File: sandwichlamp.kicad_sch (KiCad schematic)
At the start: 27 parts, among them J1 Pole1, J2 Pole2, J3 Pole3, J4 12V Enable, J5 HLK-LD2410C, J6 Conn_01x02, J7 Conn_01x03, SW1 Rader Power, SW3 POWER, U1 magnetic-charger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

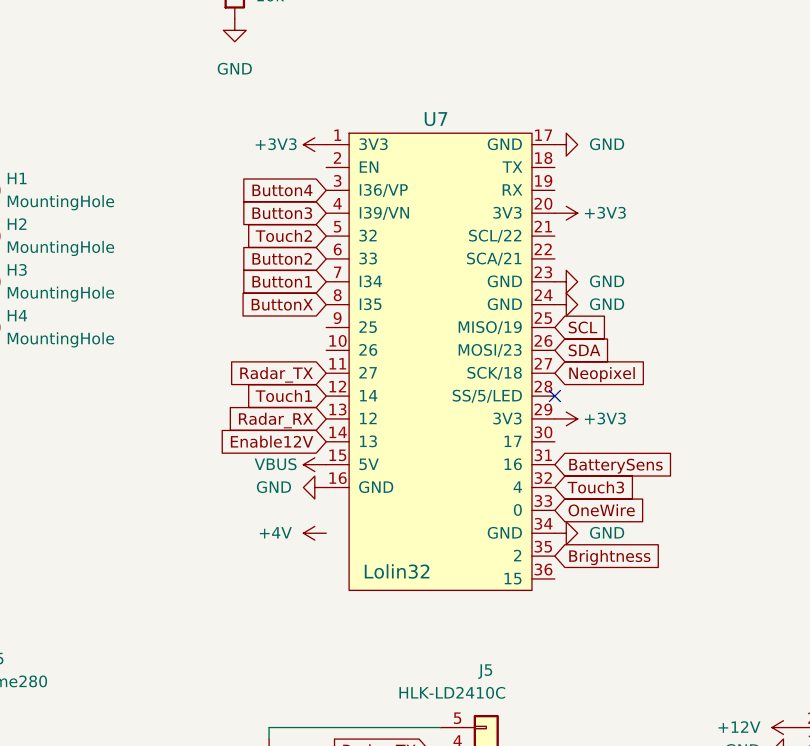
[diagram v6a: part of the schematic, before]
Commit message: Cleanup schematic and pcb
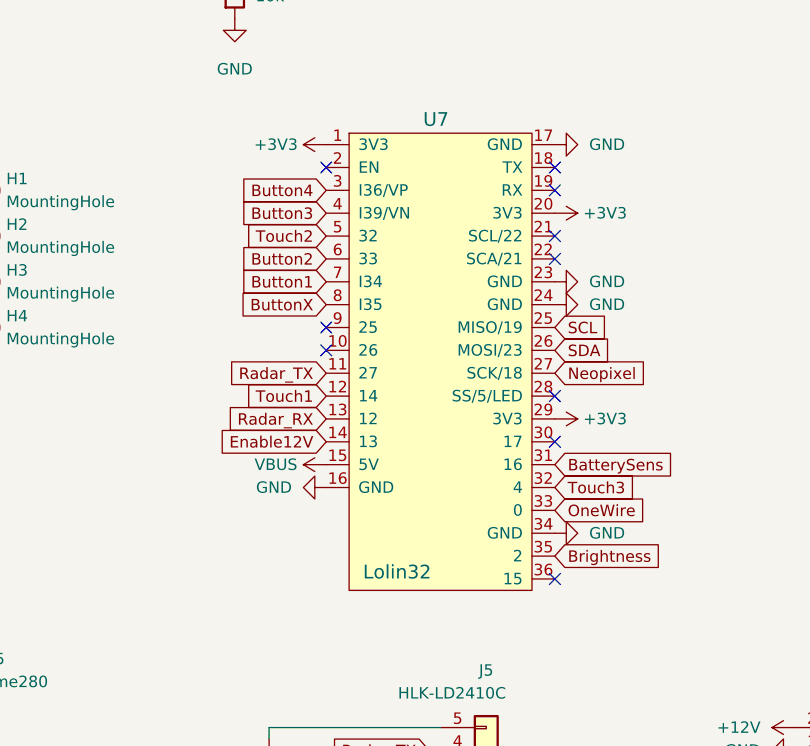
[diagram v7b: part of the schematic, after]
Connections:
- no-connect marks 3 -> 12
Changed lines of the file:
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@@
 	)
 	(no_connect
+		(at 130.81 80.01)
+	)
+	(no_connect
 		(at 31.75 60.96)
 	)
@@
 		(at 156.21 85.09)
 	)
+	(no_connect
+		(at 156.21 105.41)
+	)
+	(no_connect
+		(at 156.21 59.69)
+	)
+	(no_connect
+		(at 156.21 69.85)
+	)
+	(no_connect
+		(at 130.81 77.47)
+	)
+	(no_connect
+		(at 156.21 67.31)
+	)
+	(no_connect
+		(at 130.81 59.69)
+	)
+	(no_connect
+		(at 156.21 62.23)
+	)
+	(no_connect
+		(at 156.21 90.17)
+	)
 	(wire
 		(pts
@@
 					(unit 1)
 				)
-			)
-		)
-	)
-	(symbol
-		(lib_id "power:+4V")
-		(at 130.81 100.33 90)
-		(unit 1)
-		(exclude_from_sim no)
-		(in_bom yes)
-		(on_board yes)
-		(dnp no)
-		(fields_autoplaced yes)
-		(property "Reference" "#PWR015"
-			(at 134.62 100.33 0)
-			(effects
-				(font
-					(size 1.27 1.27)
-				)
-				(hide yes)
-			)
-		)
-		(property "Value" "+4V"
-			(at 127 100.3301 90)
-			(effects
-				(font
-					(size 1.27 1.27)
-				)
-				(justify left)
-			)
-		)
-		(property "Footprint" ""
-			(at 130.81 100.33 0)
-			(effects
-				(font
-					(size 1.27 1.27)
-				)
-				(hide yes)
-			)
-		)
-		(property "Datasheet" ""
-			(at 130.81 100.33 0)
-			(effects
-				(font
-					(size 1.27 1.27)
-				)
-				(hide yes)
-			)
-		)
-		(property "Description" "Power symbol creates a global label with name \"+4V\""
-			(at 130.81 100.33 0)
-			(effects
-				(font
-					(size 1.27 1.27)
-				)
-				(hide yes)
-			)
-		)
-		(pin "1"
-		)
-		(instances
-			(project "sandwichlamp"
-				(path "/e0ec050d-3d79-41e4-bfa7-38c68df5e8aa"
-					(reference "#PWR015")
-					(unit 1)
-				)

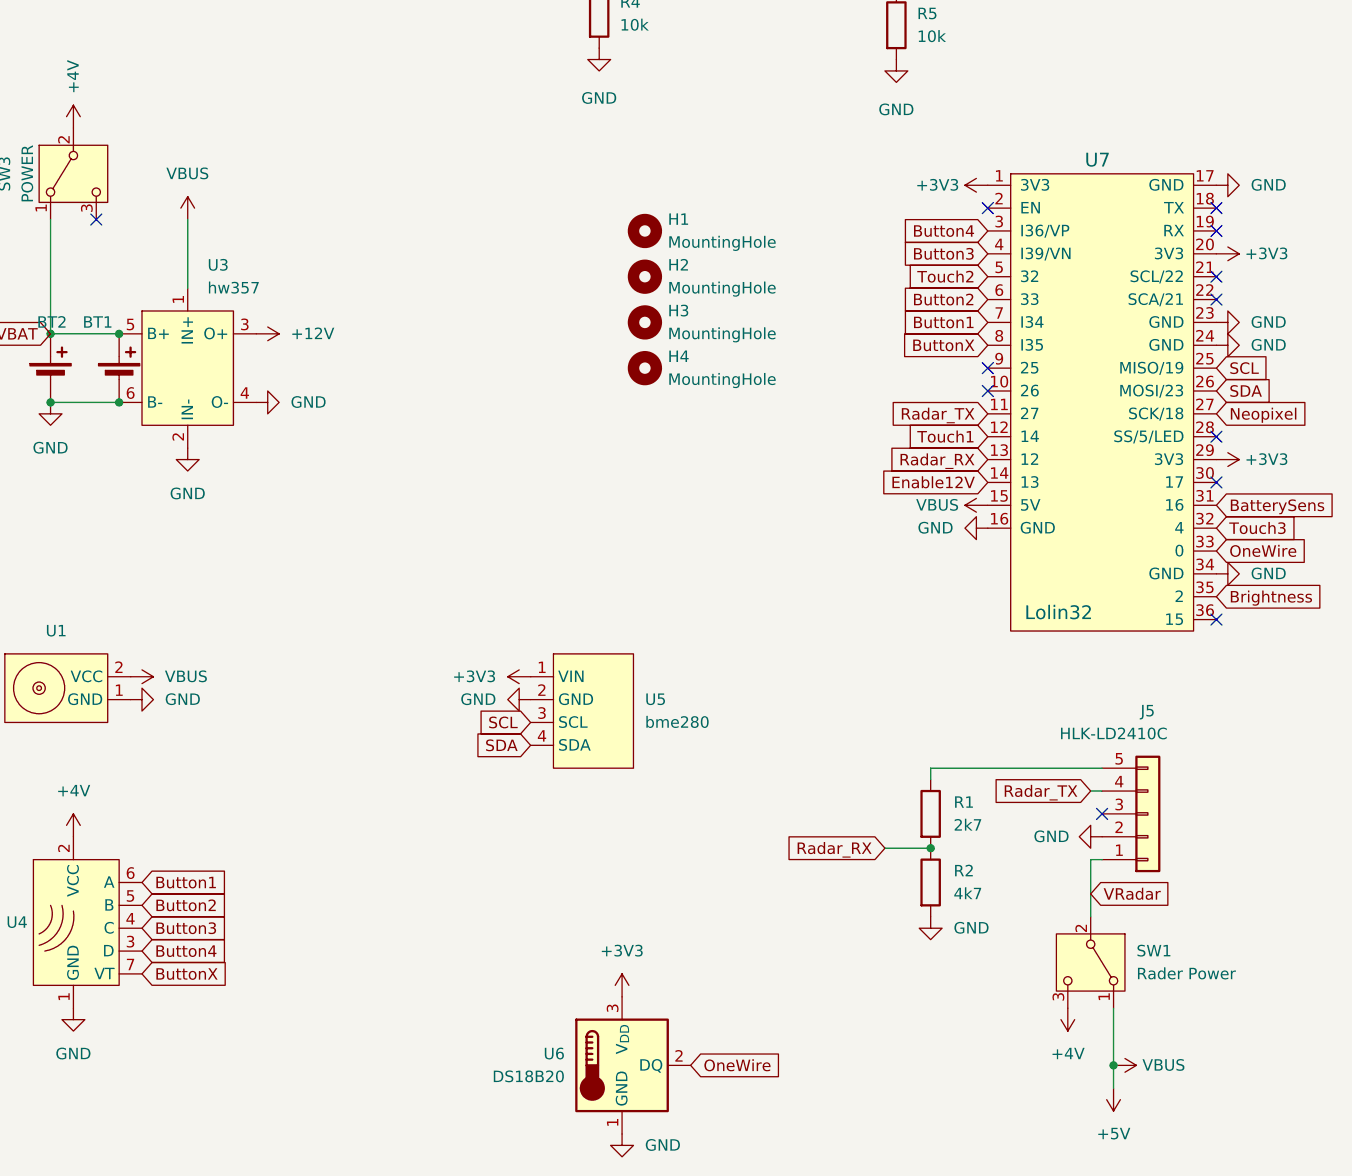
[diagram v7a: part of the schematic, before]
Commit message: Disconnect the two 5V nets from one another
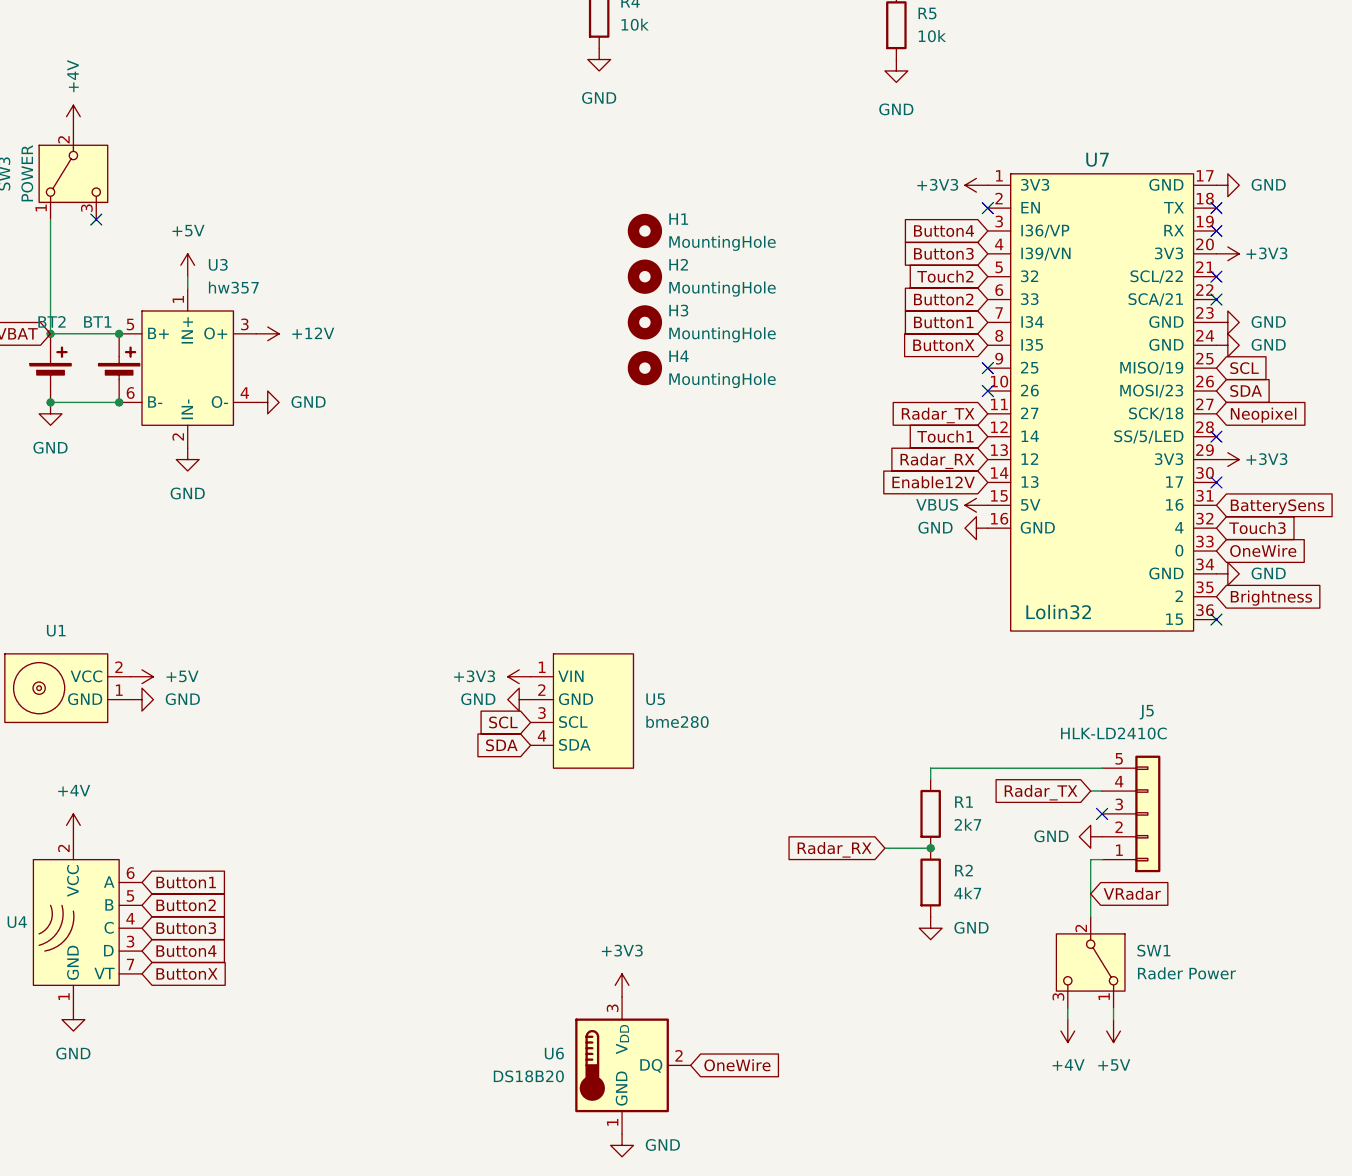
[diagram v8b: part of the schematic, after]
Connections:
- net +5V: no longer U7.15 (5V)
- new net VBUS: U7.15 (5V)
